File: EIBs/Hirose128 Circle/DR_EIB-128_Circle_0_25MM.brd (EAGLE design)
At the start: 38.6 x 38.6 mm, 42 parts

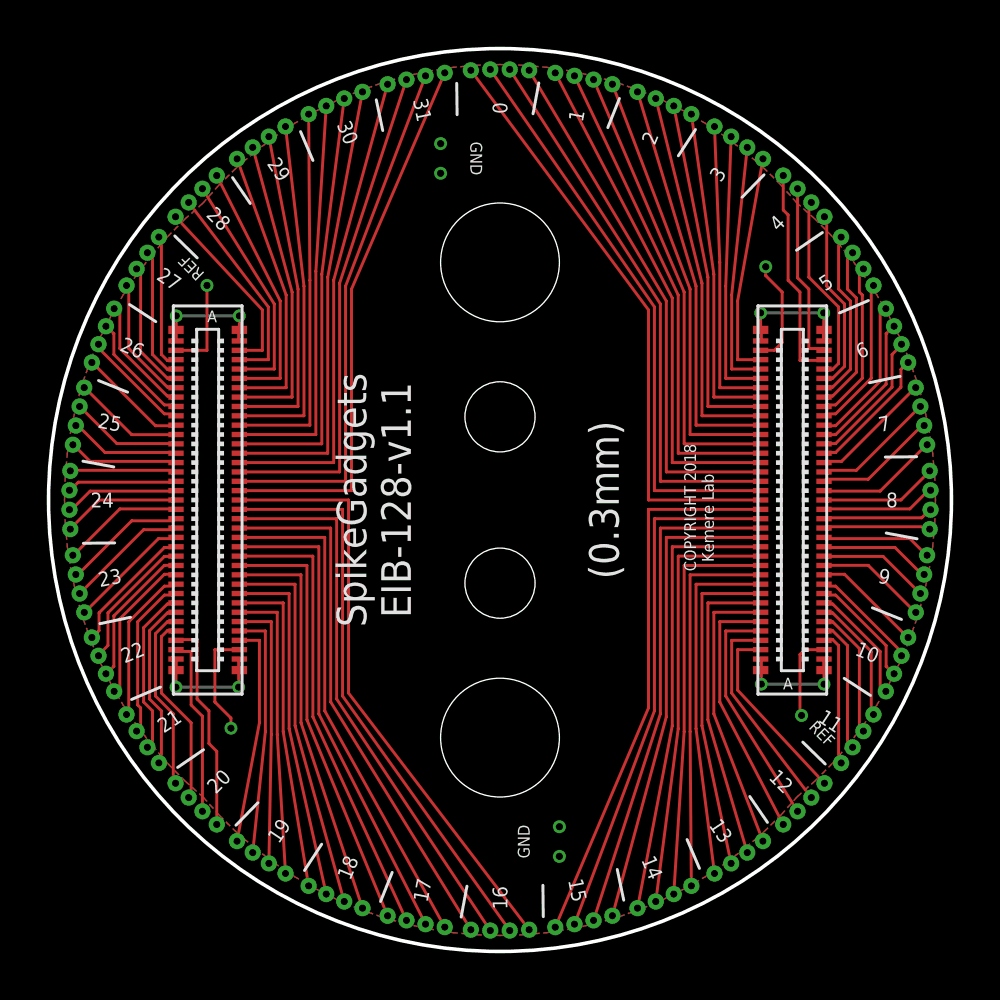
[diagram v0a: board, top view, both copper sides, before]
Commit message: Three updates for Circular EIB: - Add library with the radial tetrode configuration (1.5 in diameter) in 0.3 mm and 0.25 mm tetrode holes - Update CircleEIB files with 0.3 mm tetrode hole specification (also update DRC with 0.3 mm minimum drill) - Add second CircleEIB files with 0.25 mm tetrode holes
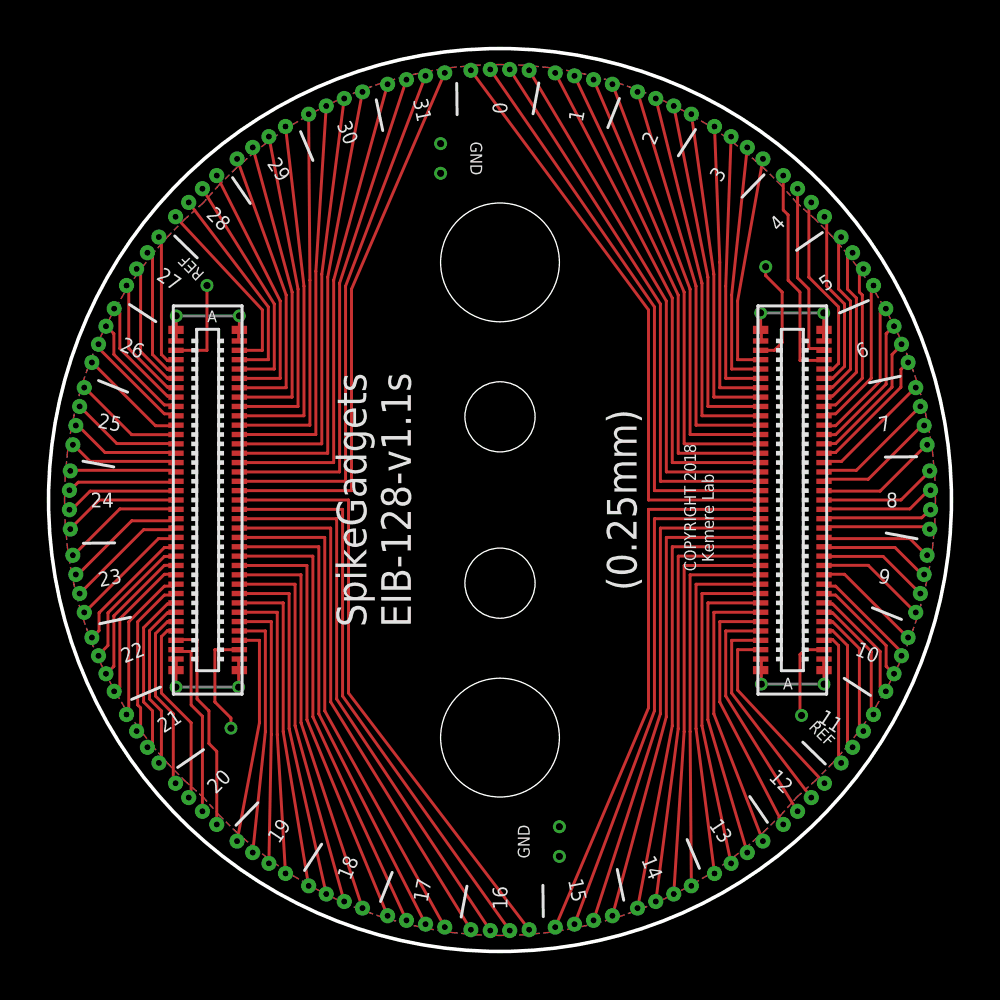
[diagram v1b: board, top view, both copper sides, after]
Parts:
- 0, 1, 10, 11, 12, 13, 14, 15, 16, 17, 18, 19, 2, 20, 21, 22, 23, 24, 25, 26, 27, 28, 29, 3, 30, 31, 4, 5, 6, 7, 8, 9: value TETRODE_1.5IN_RADIUS0.3MM -> TETRODE_1.5IN_RADIUS0.25MM; device CactusPinInterfaces:TETRODE_1.5IN_RADIUS_0.3MM -> CactusPinInterfaces:TETRODE_1.5IN_RADIUS_0.25MM
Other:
- board text added: "(0.25mm)"
- board text added: "SpikeGadgets EIB-128-v1.1s"
- board text removed: "(0.3mm)"
- board text removed: "SpikeGadgets EIB-128-v1.1"
